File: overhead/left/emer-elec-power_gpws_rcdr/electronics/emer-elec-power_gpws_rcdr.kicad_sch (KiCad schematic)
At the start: 84 parts, among them J1 Conn_02x01, J2 Conn_02x13_Counter_Clockwise, J3 Conn_02x01, J4 Conn_02x01, J5 Conn_02x01, J6 Conn_02x01

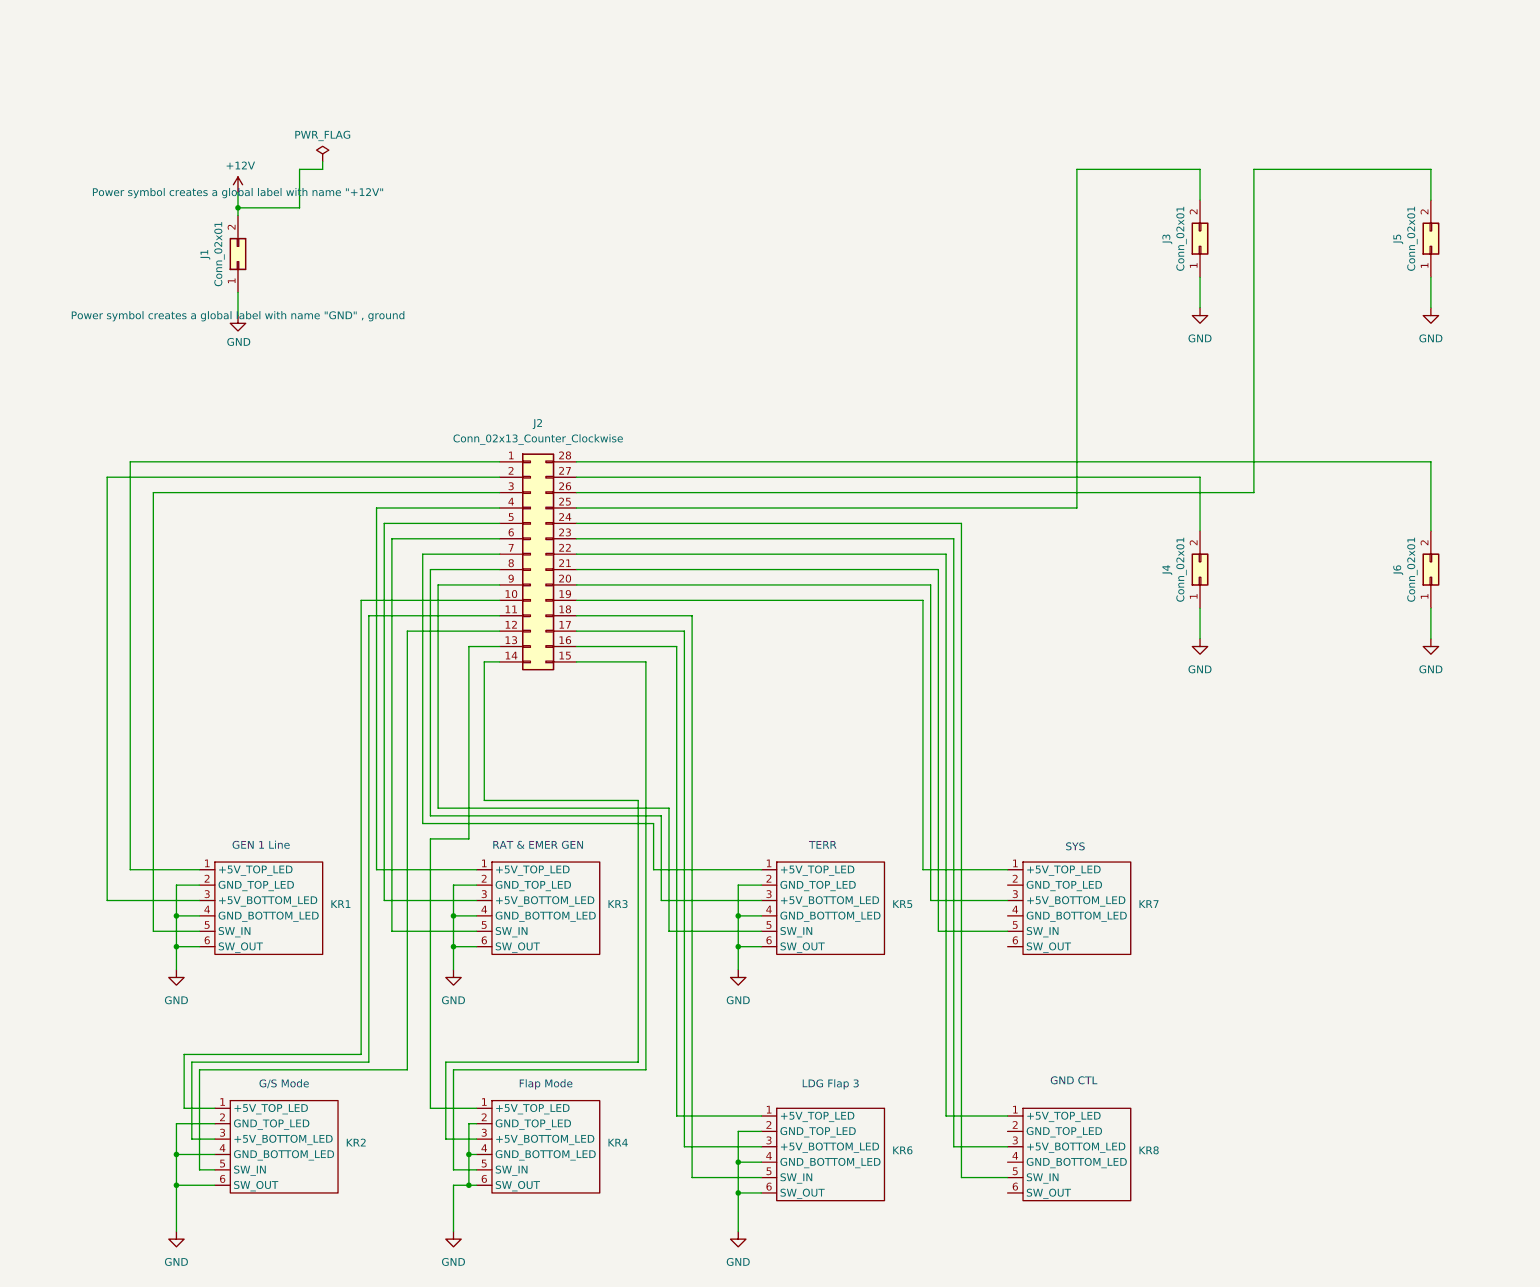
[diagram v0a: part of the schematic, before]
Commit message: Updated PCB Iteration 2 for Emer Elec Panel
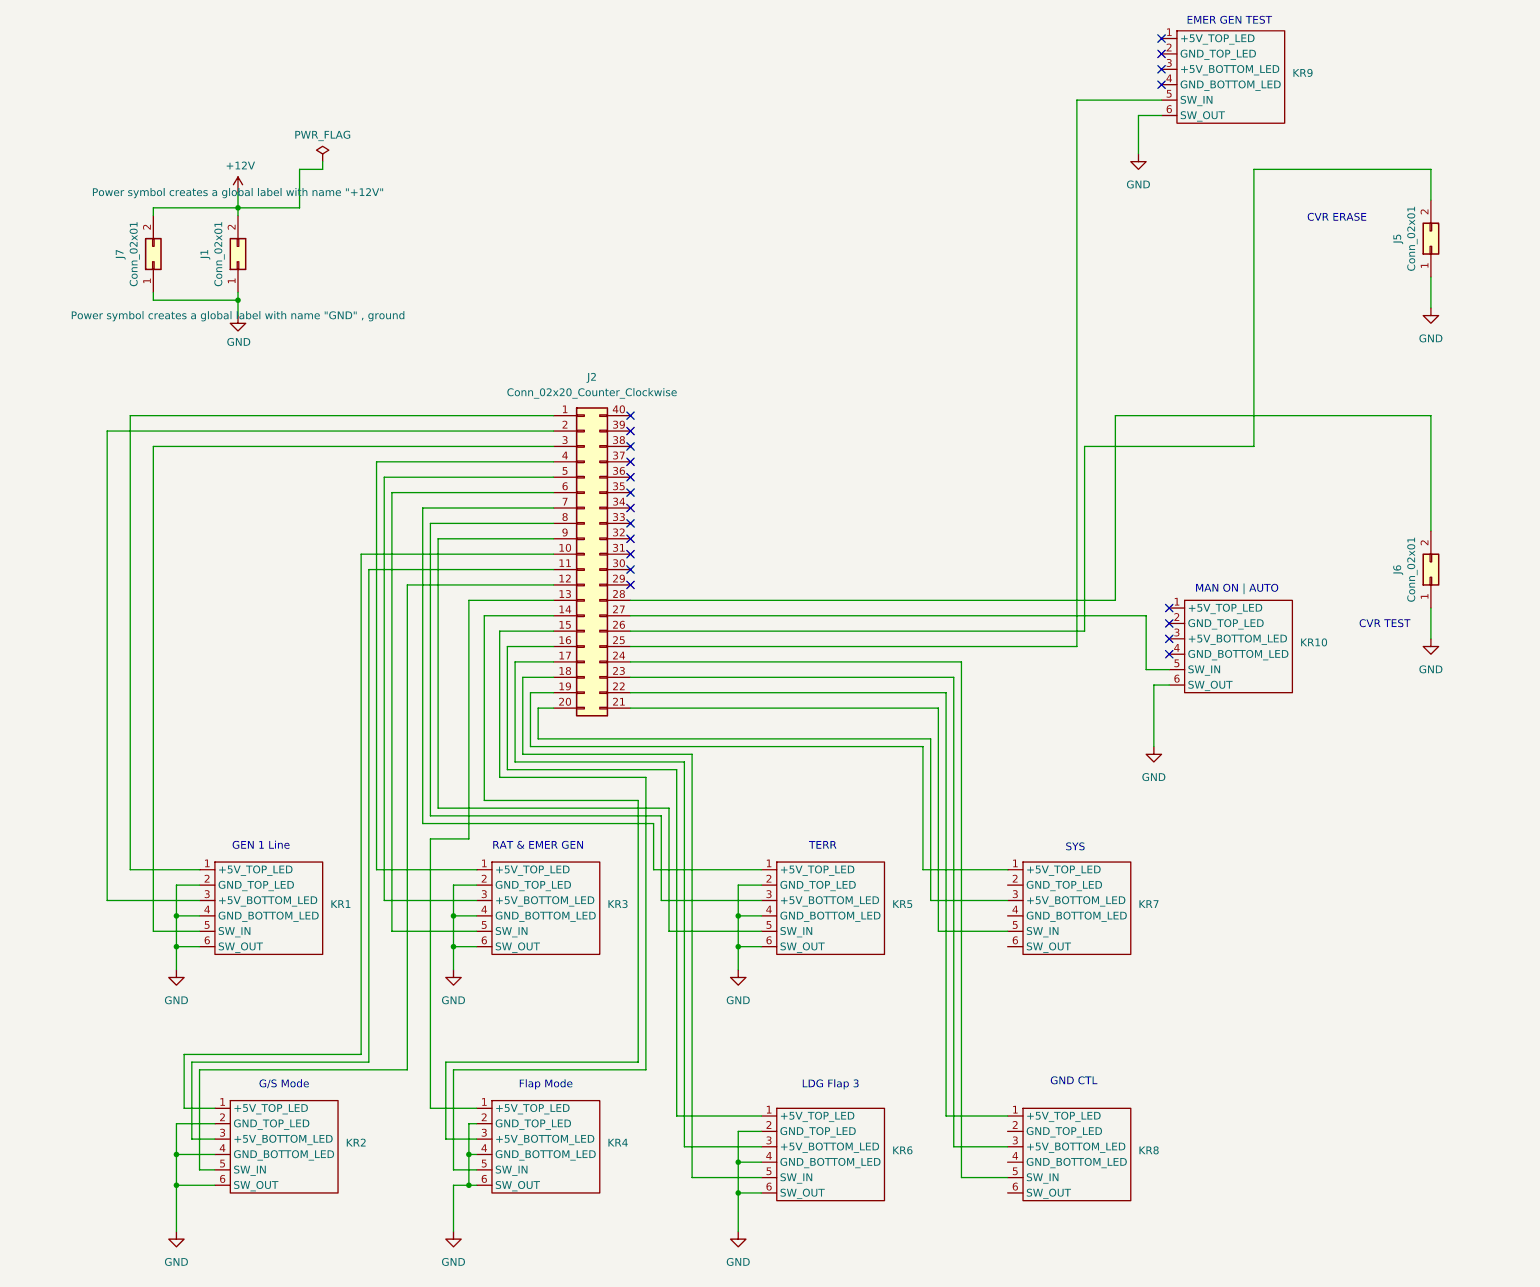
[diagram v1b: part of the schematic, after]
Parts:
- removed J2: Conn_02x13_Counter_Clockwise, Connector_PinHeader_2.54mm:PinHeader_2x14_P2.54mm_Vertical, symbol Connector_Generic:Conn_02x14_Counter_Clockwise
- removed J3, J4: Conn_02x01, Connector_PinHeader_2.54mm:PinHeader_1x02_P2.54mm_Vertical, symbol Connector_Generic:Conn_02x01
- added J2: Conn_02x20_Counter_Clockwise, Connector_PinHeader_2.54mm:PinHeader_2x20_P2.54mm_Vertical, symbol Connector_Generic:Conn_02x20_Counter_Clockwise
- added J7: Conn_02x01, TerminalBlock:TerminalBlock_bornier-2_P5.08mm, symbol Connector_Generic:Conn_02x01
- added KR10, KR9: ~, OpenA3XX:Korry Switch, symbol KorrySwitch:Korry_Switch
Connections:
- net +12V: now also J7.2 (Pin_2)
- net GND: now also J7.1 (Pin_1), KR10.6 (SW_OUT), KR9.6 (SW_OUT)
- net at KR4.1 (+5V_TOP_LED): now also J2.13 (Pin_13)
- net at KR4.3 (+5V_BOTTOM_LED): now also J2.14 (Pin_14)
- net at KR4.5 (SW_IN): now also J2.15 (Pin_15)
- net at J5.2 (Pin_2): now also J2.26 (Pin_26)
- net at J6.2 (Pin_2): now also J2.28 (Pin_28)
- net at KR1.1 (+5V_TOP_LED): now also J2.1 (Pin_1)
- net at KR2.1 (+5V_TOP_LED): now also J2.10 (Pin_10)
- net at KR2.3 (+5V_BOTTOM_LED): now also J2.11 (Pin_11)
- net at KR2.5 (SW_IN): now also J2.12 (Pin_12)
- net at KR6.1 (+5V_TOP_LED): now also J2.16 (Pin_16)
- net at KR6.3 (+5V_BOTTOM_LED): now also J2.17 (Pin_17)
- net at KR6.5 (SW_IN): now also J2.18 (Pin_18)
- net at KR7.1 (+5V_TOP_LED): now also J2.19 (Pin_19)
- net at KR1.3 (+5V_BOTTOM_LED): now also J2.2 (Pin_2)
- net at KR7.3 (+5V_BOTTOM_LED): now also J2.20 (Pin_20)
- net at KR7.5 (SW_IN): now also J2.21 (Pin_21)
- net at KR8.1 (+5V_TOP_LED): now also J2.22 (Pin_22)
- net at KR8.3 (+5V_BOTTOM_LED): now also J2.23 (Pin_23)
- net at KR8.5 (SW_IN): now also J2.24 (Pin_24)
- net at KR1.5 (SW_IN): now also J2.3 (Pin_3)
- net at KR3.1 (+5V_TOP_LED): now also J2.4 (Pin_4)
- net at KR3.3 (+5V_BOTTOM_LED): now also J2.5 (Pin_5)
- net at KR3.5 (SW_IN): now also J2.6 (Pin_6)
- net at KR5.1 (+5V_TOP_LED): now also J2.7 (Pin_7)
- net at KR5.3 (+5V_BOTTOM_LED): now also J2.8 (Pin_8)
- net at KR5.5 (SW_IN): now also J2.9 (Pin_9)
- new net: J2.25 (Pin_25), KR9.5 (SW_IN)
- new net: J2.27 (Pin_27), KR10.5 (SW_IN)
- no-connect marks 0 -> 20
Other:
- note added: "CVR ERASE"
- note added: "CVR TEST"
- note added: "EMER GEN TEST"
- note added: "MAN ON | AUTO"
